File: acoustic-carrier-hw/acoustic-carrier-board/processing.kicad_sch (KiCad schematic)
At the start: 25 parts, among them IC1 ECP5-BGA256, J2 Conn_01x04_Socket, J4 Conn_01x06_Socket, J5 Conn_01x02_Socket, U4 W25Q128JVS, U9 W25Q128JVS

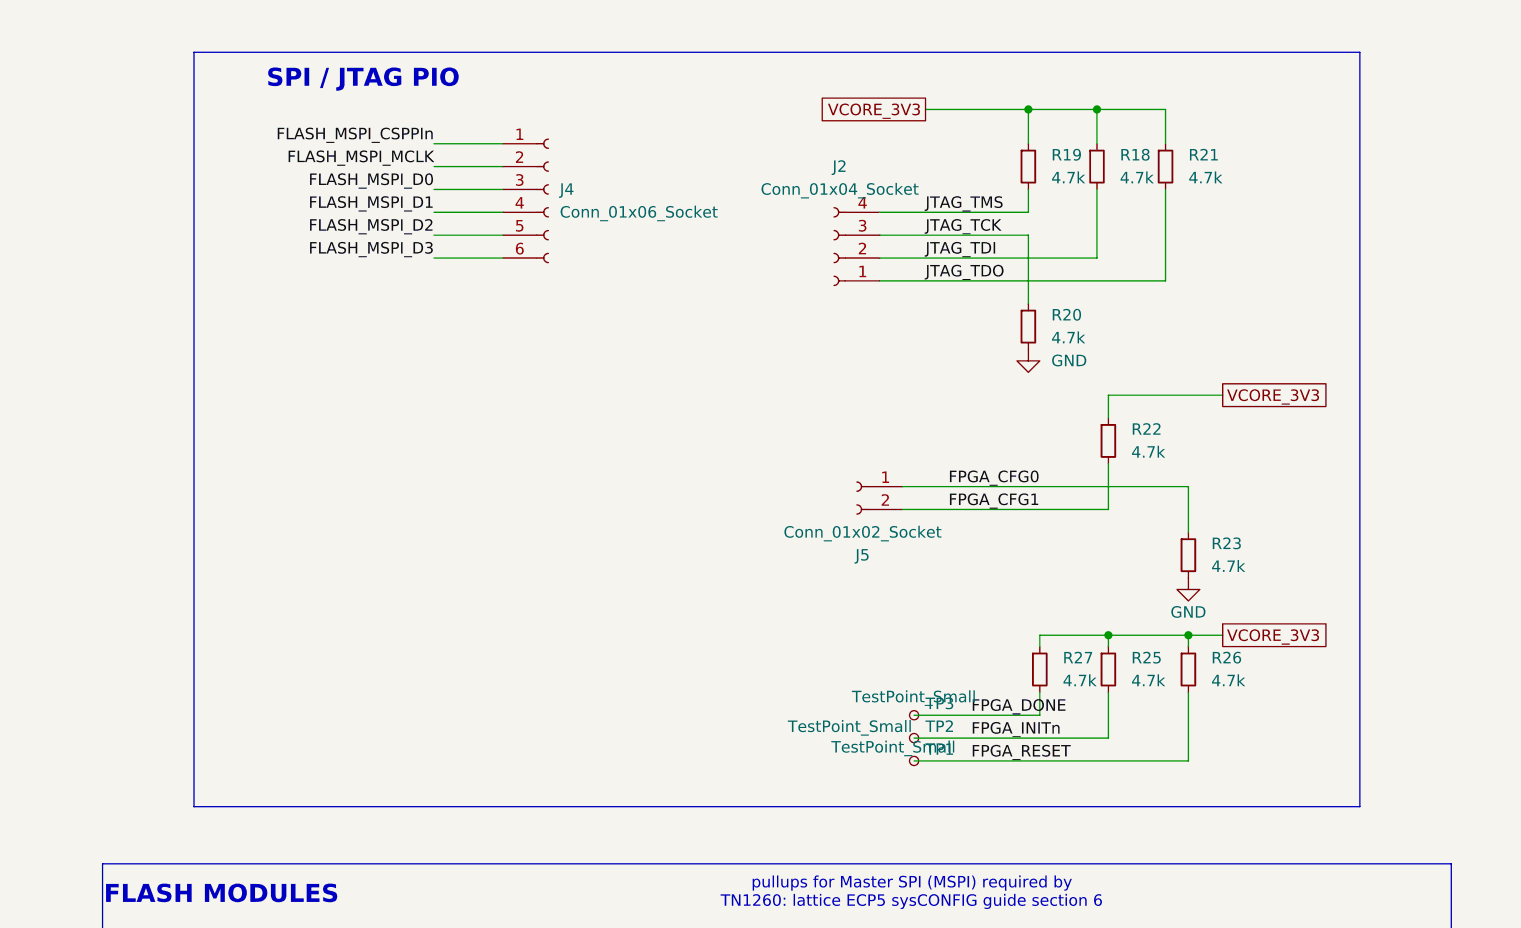
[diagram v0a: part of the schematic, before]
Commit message: [carrier] Fixed ERC errors and fpga-footprints (next) ) add extra pin functionality to 2 remaining banks, perform schematic checks
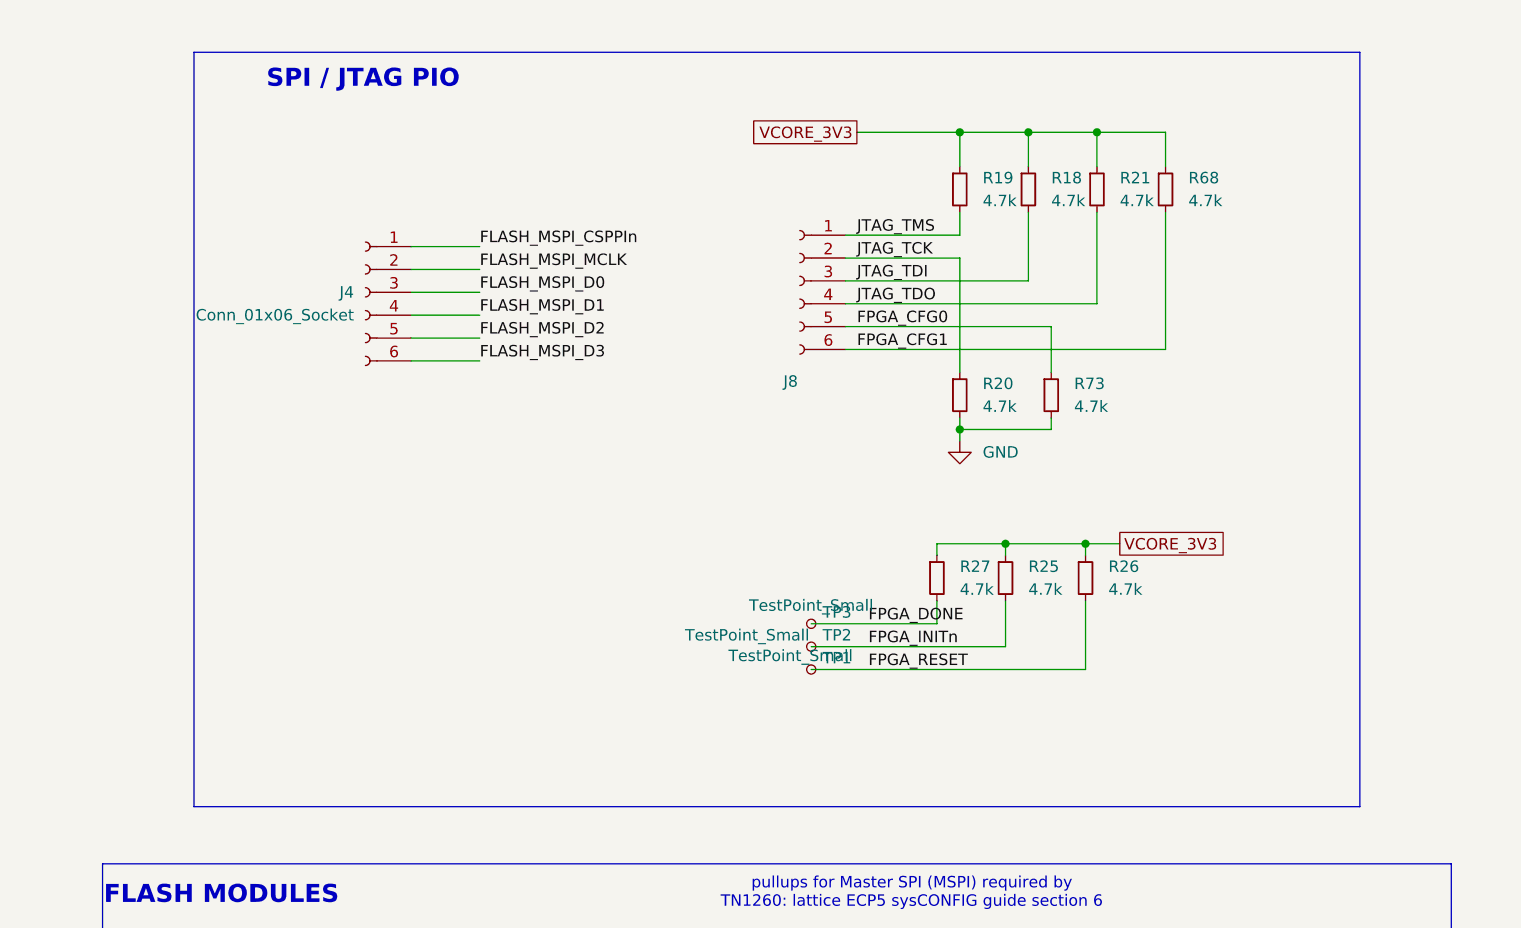
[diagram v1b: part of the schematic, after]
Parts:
- removed J2: Conn_01x04_Socket, symbol Connector:Conn_01x04_Socket
- removed J5: Conn_01x02_Socket, symbol Connector:Conn_01x02_Socket
- removed R22, R23: 4.7k, Resistor_SMD:R_0402_1005Metric, symbol Device:R_Small
- added J8: Conn_01x06_Socket, Connector_PinHeader_1.27mm:PinHeader_1x06_P1.27mm_Vertical, symbol Connector:Conn_01x06_Socket
- added R68, R73: 4.7k, Resistor_SMD:R_0402_1005Metric, symbol Device:R_Small
- IC1: Part Number LFE5U-25F-6BG256C -> (none)
- J4: footprint (none) -> Connector_PinHeader_1.27mm:PinHeader_1x06_P1.27mm_Vertical; LPN (none) -> C2832269; MPN (none) -> PM254V-11-06-H85
- TP1, TP2, TP3: footprint (none) -> TestPoint:TestPoint_Pad_D1.5mm
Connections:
- net FPGA_CFG0: now also J8.5 (Pin_5), R73.1
- net FPGA_CFG1: now also J8.6 (Pin_6), R68.2
- net GND: now also R73.2
- net JTAG_TCK: now also J8.2 (Pin_2)
- net JTAG_TDI: now also J8.3 (Pin_3)
- net JTAG_TDO: now also J8.4 (Pin_4)
- net JTAG_TMS: now also J8.1 (Pin_1)
- net VCORE_3V3: now also R68.1
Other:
- moved on the sheet: J4, R18, R19, R20, R21, R25, R26, R27, TP1, TP2, TP3
